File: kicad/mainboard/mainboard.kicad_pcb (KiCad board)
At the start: 2 copper layers, 40 x 58 mm, 32 parts, among them J1 USB_C_Receptacle_USB2.0_16P, J2 Conn_01x07_Socket, J3 Conn_01x06_Socket, J4 Conn_01x03_Socket, J5 Conn_01x07_Socket, SW1 FSM2JSMAATR, SW2 FSM2JSMAATR, U1 TPD1E05U06DYA, U2 TPD1E05U06DYA, U3 ESP32-S3-WROOM-1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

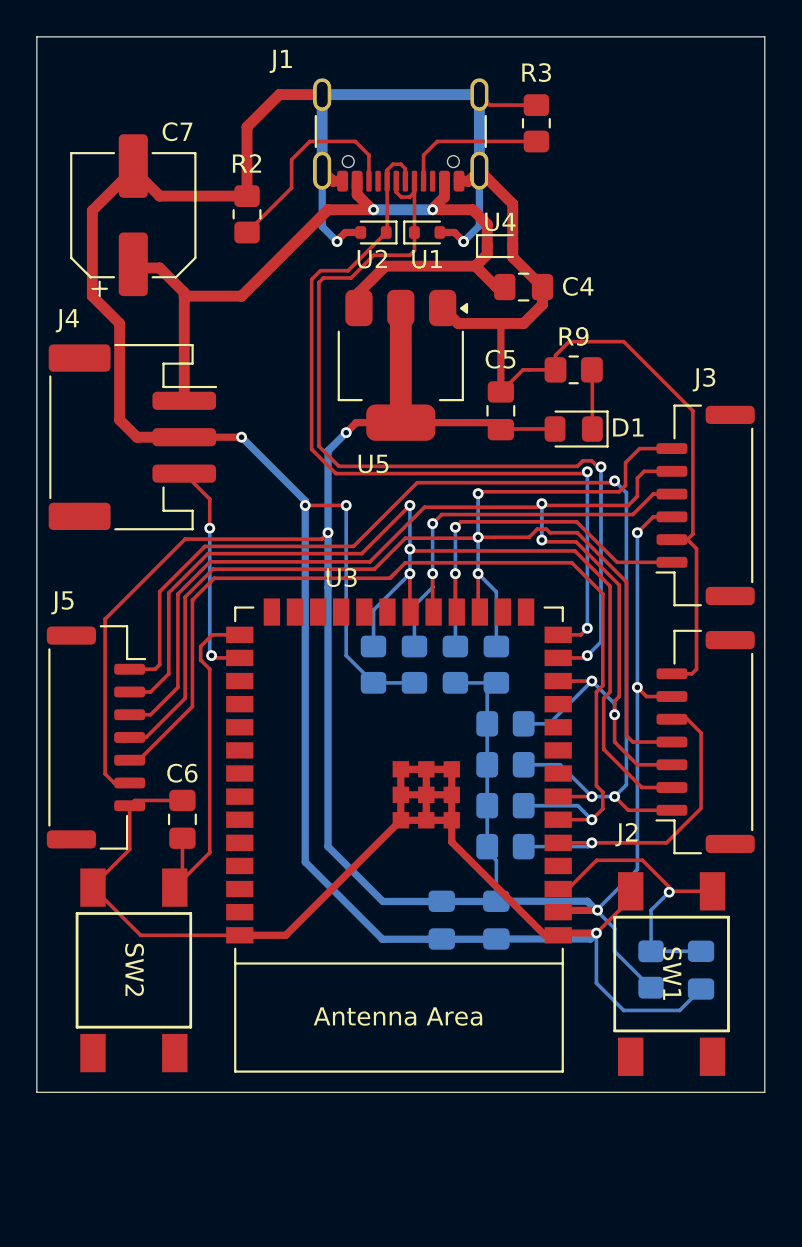
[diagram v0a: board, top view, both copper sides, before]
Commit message: via/trace cleanup, larger via for 5v2a
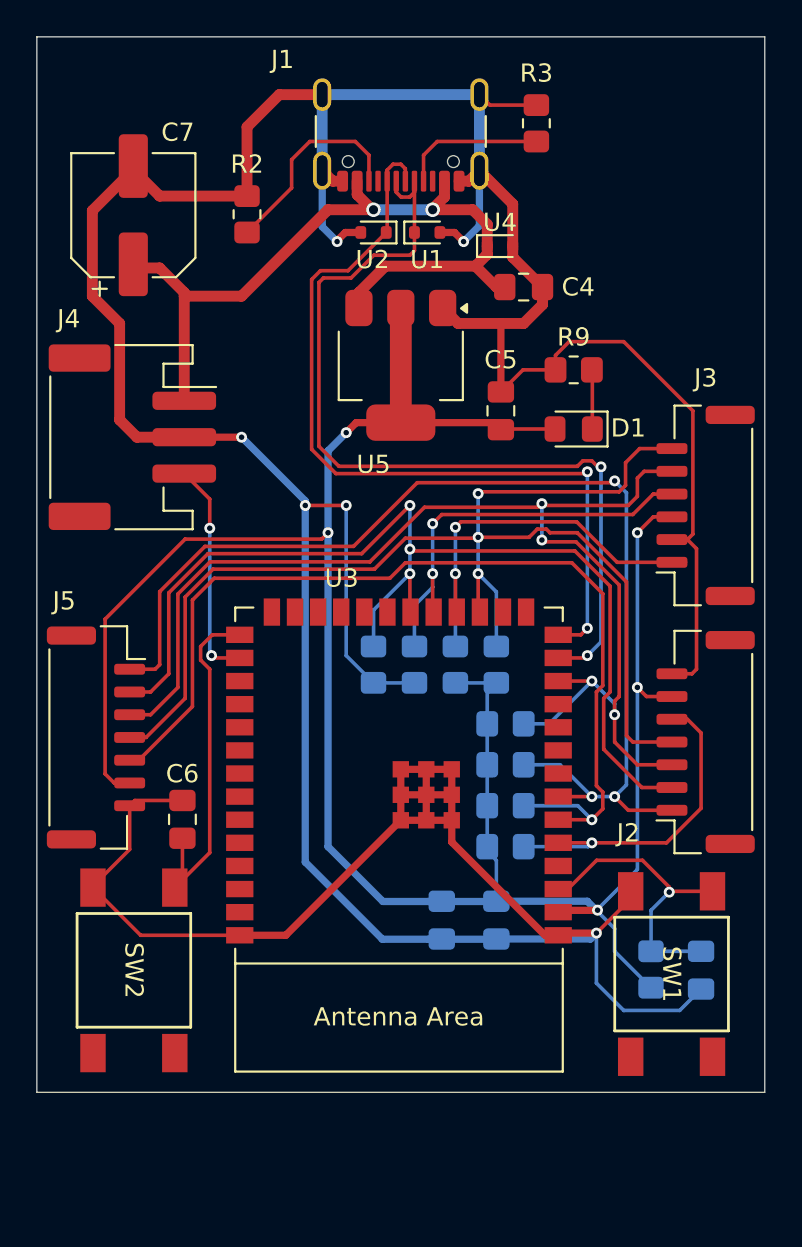
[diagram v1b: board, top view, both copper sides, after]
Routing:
- net +3.3V: track 131.0 -> 130.2 mm
- net GND: track 249.9 -> 249.3 mm
- net SMCLK: track 71.5 -> 71.0 mm
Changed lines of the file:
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@@
-	)
-	(segment
-		(start 136.88215 110.7034)
-		(end 136.88215 110.574088)
-		(width 0.2)
-		(layer "F.Cu")
-		(net 1)
 	)
 	(segment
@@
 	)
 	(segment
-		(start 109.35 106)
-		(end 109.75 106)
-		(width 0.2)
-		(layer "F.Cu")
-		(net 1)
-	)
-	(segment
 		(start 124.25 106.8)
 		(end 124.25 104)
@@
 	)
 	(segment
-		(start 132.75 82.05)
-		(end 131.3 82.05)
+		(start 130.9625 82.05)
+		(end 132.75 82.05)
 		(width 0.2)
 		(layer "F.Cu")
@@
 	)
 	(segment
-		(start 131.3 82.05)
-		(end 130.9625 82.05)
-		(width 0.2)
-		(layer "F.Cu")
-		(net 1)
-	)
-	(segment
 		(start 115.8 72.5)
 		(end 111 72.5)
@@
 		(end 128.57 71.105)
 		(width 0.6)
-		(layer "B.Cu")
-		(net 1)
-	)
-	(segment
-		(start 120.7 75)
-		(end 120.75 75)
-		(width 0.4)
 		(layer "B.Cu")
 		(net 1)
@@
 	)
 	(segment
-		(start 123.7 85.5)
-		(end 124.25 84.95)
-		(width 0.4)
-		(layer "F.Cu")
-		(net 3)
-	)
-	(segment
 		(start 129.7875 85.3)
 		(end 129.75 85.3375)
@@
 	(segment
 		(start 120.25 108.25)
-		(end 120.25 94)
+		(end 120.25 86.5)
 		(width 0.4)
 		(layer "B.Cu")
@@
 	)
 	(segment
-		(start 120.25 94)
-		(end 120.25 86.5)
-		(width 0.4)
-		(layer "B.Cu")
-		(net 3)
-	)
-	(segment
 		(start 127.25 99.25)
 		(end 129.5 99.25)
@@
 	)
 	(segment
-		(start 128.6 76.1)
-		(end 128.35 76.35)
+		(start 128.35 76.35)
+		(end 129 75.7)
 		(width 0.6)
 		(layer "F.Cu")
@@
 	)
 	(segment
-		(start 129 75.7)
-		(end 128.6 76.1)
-		(width 0.6)
-		(layer "F.Cu")
-		(net 4)
-	)
-	(segment
 		(start 129.5 77.5)
 		(end 129.9625 77.5)
@@
 	(via
 		(at 126 73.25)
-		(size 0.6)
-		(drill 0.3)
+		(size 0.8)
+		(drill 0.5)
 		(layers "F.Cu" "B.Cu")
 		(net 4)
@@
 	(via
 		(at 122.75 73.25)
-		(size 0.6)
-		(drill 0.3)
+		(size 0.8)
+		(drill 0.5)
 		(layers "F.Cu" "B.Cu")
 		(net 4)
@@
 	)
 	(segment
-		(start 111.75 110.419375)
-		(end 111.830625 110.5)
-		(width 0.2)
-		(layer "F.Cu")
-		(net 5)
-	)
-	(segment
 		(start 113.75 98.498529)
 		(end 113.75 108.580625)
@@
 	)
 	(segment
-		(start 128.595 94.83)
-		(end 128.595 95.36)
-		(width 0.2)
-		(layer "F.Cu")
-		(net 15)
-	)
-	(segment
 		(start 131.301471 91.25)
 		(end 131.751471 90.8)
@@
 	)
 	(segment
-		(start 123.950735 93.200735)
+		(start 123.65147 93.5)
 		(end 124.501471 92.65)
 		(width 0.2)
@@
 	)
 	(segment
-		(start 123.651471 93.5)
-		(end 123.950735 93.200735)
-		(width 0.2)
-		(layer "F.Cu")
-		(net 18)
-	)
-	(segment
 		(start 133.65 92.65)
 		(end 135.35 94.35)
@@
 		(width 0.2)
 		(layer "F.Cu")
-		(net 18)
-	)
-	(segment
-		(start 123.65147 93.5)
-		(end 123.950735 93.200735)
-		(width 0.2)
-		(layer "F.Cu")

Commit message: adjust edge cut
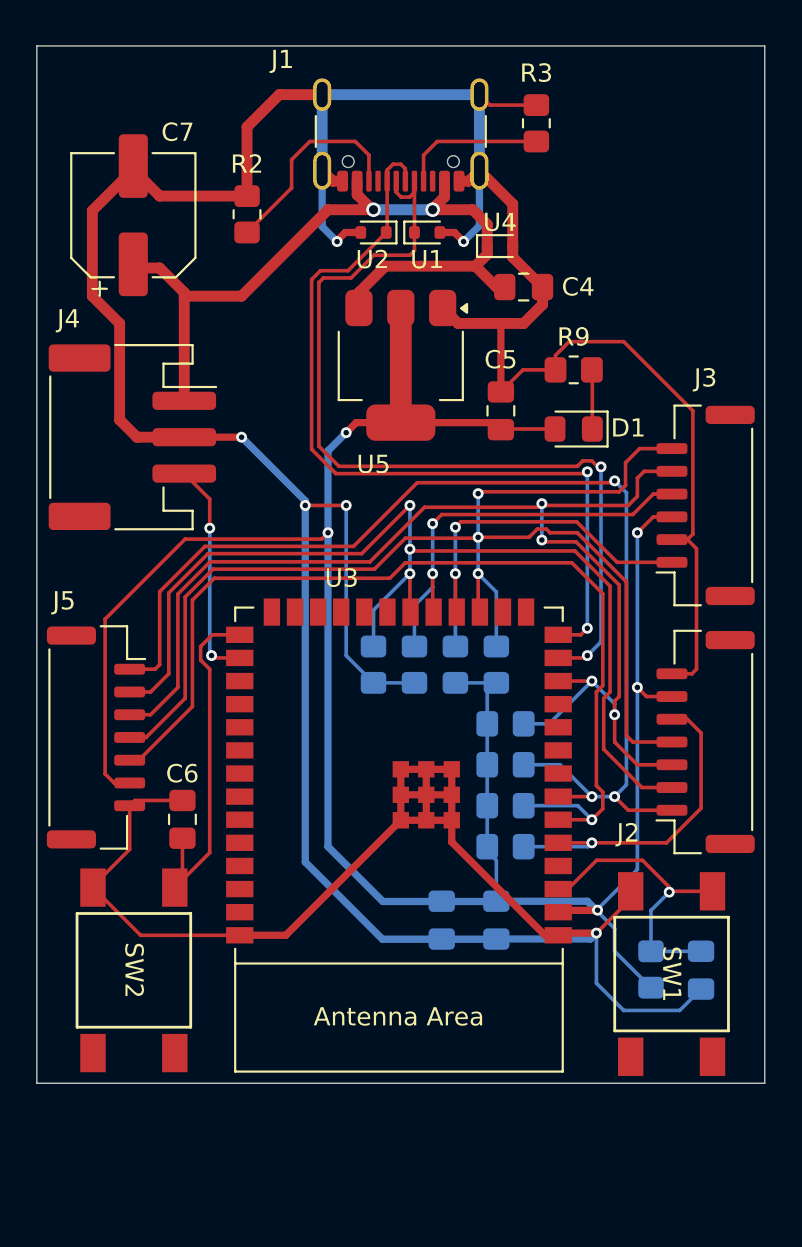
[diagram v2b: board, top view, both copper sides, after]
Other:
- board size 40 x 58 mm -> 40 x 57 mm
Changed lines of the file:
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@@
 	)
 	(gr_line
-		(start 144.25 60.25)
-		(end 124.25 60.25)
+		(start 144.25 65.25)
+		(end 124.25 65.25)
 		(stroke
 			(width 0.1)
@@
 	)
 	(gr_line
-		(start 124.25 60.25)
-		(end 124.25 57.75)
+		(start 124.25 65.25)
+		(end 124.25 62.75)
 		(stroke
 			(width 0.1)
@@
 	)
 	(gr_rect
-		(start 104.25 63.75)
-		(end 144.25 121.75)
+		(start 104.25 64.25)
+		(end 144.25 121.25)
 		(stroke
 			(width 0.05)

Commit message: Add logo
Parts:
- added G***: LOGO, Logo:Snep, F.Cu at (139.0, 69.0)

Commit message: fix erc
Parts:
- moved SW1 0.20 mm to (141.4, 110.5)
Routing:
- net EN: track 16.5 -> 17.2 mm
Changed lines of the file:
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@@
 		(tags "USB C Type-C Receptacle SMD USB 2.0 16P 16C USB4105-15-A USB4105-15-A-060 USB4105-15-A-120 USB4105-GF-A USB4105-GF-A-060 USB4105-GF-A-120")
 		(property "Reference" "J1"
-			(at 6.5 3 0)
+			(at 6.5 2.5 0)
 			(unlocked yes)
 			(layer "F.SilkS")
@@
 		(tags "capacitor handsolder")
 		(property "Reference" "C6"
-			(at -2.5 0 180)
+			(at -2.75 0 180)
 			(layer "F.SilkS")
 			(effects
@@
 		(tags "connector JST GH horizontal")
 		(property "Reference" "J2"
-			(at -5 -4.25 180)
+			(at 6 -4.25 180)
 			(layer "F.SilkS")
 			(effects
@@
 	(footprint "FSM2JSMAATR:SWITCH_FSM2JSMAA_TYC"
 		(layer "F.Cu")
-		(at 141.37795 110.7034 -90)
+		(at 141.37795 110.5 -90)
 		(tags "FSM2JSMAATR ")
 		(property "Reference" "SW1"
@@
 		(tags "resistor handsolder")
 		(property "Reference" "R11"
-			(at -2.75 -0.5 0)
+			(at -0.25 -2.5 0)
 			(layer "B.SilkS")
 			(effects
@@
 		(tags "resistor handsolder")
 		(property "Reference" "R12"
-			(at -2.75 0.25 0)
+			(at -2.75 0 0)
 			(layer "B.SilkS")
 			(effects
@@
 	)
 	(segment
+		(start 136.88215 111.11785)
+		(end 136.88215 110.5)
+		(width 0.2)
+		(layer "F.Cu")
+		(net 1)
+	)
+	(segment
 		(start 125.65 104)
 		(end 125.65 106.8)
@@
 	)
 	(segment
+		(start 135 113)
+		(end 136.88215 111.11785)
+		(width 0.2)
+		(layer "F.Cu")
+		(net 1)
+	)
+	(segment
 		(start 131.7 67.5)
 		(end 129.145 67.5)
@@
 	)
 	(segment
-		(start 136.88215 110.7034)
-		(end 136.88215 111.11785)
-		(width 0.2)
-		(layer "F.Cu")
-		(net 1)
-	)
-	(segment
 		(start 130.4 75.8625)
 		(end 132.0375 77.5)
@@
 	)
 	(segment
-		(start 136.88215 111.11785)
-		(end 135 113)
-		(width 0.2)
-		(layer "F.Cu")
-		(net 1)
-	)
-	(segment
 		(start 107.3 73.3)
 		(end 107.3 78)
@@
 	)
 	(segment
-		(start 137.53135 109)
-		(end 135.01 109)
+		(start 139.25 110.5)
+		(end 141.37795 110.5)
 		(width 0.2)
 		(layer "F.Cu")
@@
 	(segment
 		(start 139 110.75)
-		(end 139 110.46865)
+		(end 139 109.75)
 		(width 0.2)
 		(layer "F.Cu")
@@
 	)
 	(segment
-		(start 139.0466 110.7034)
-		(end 141.37795 110.7034)
+		(start 139 110.75)
+		(end 139.25 110.5)
 		(width 0.2)
 		(layer "F.Cu")
@@
 	)
 	(segment
-		(start 139 110.75)
-		(end 139.0466 110.7034)
+		(start 138 108.75)
+		(end 135.26 108.75)
 		(width 0.2)
 		(layer "F.Cu")
@@
 	)
 	(segment
-		(start 139 110.46865)
-		(end 137.53135 109)
+		(start 139 109.75)
+		(end 138 108.75)
 		(width 0.2)
 		(layer "F.Cu")
@@
 	)
 	(segment
-		(start 135.01 109)
-		(end 133.43 110.58)
+		(start 133.43 110.58)
+		(end 132.9 110.58)
 		(width 0.2)
 		(layer "F.Cu")
@@
 	)
 	(segment
-		(start 133.43 110.58)
-		(end 132.9 110.58)
+		(start 135.26 108.75)
+		(end 133.43 110.58)
 		(width 0.2)
 		(layer "F.Cu")

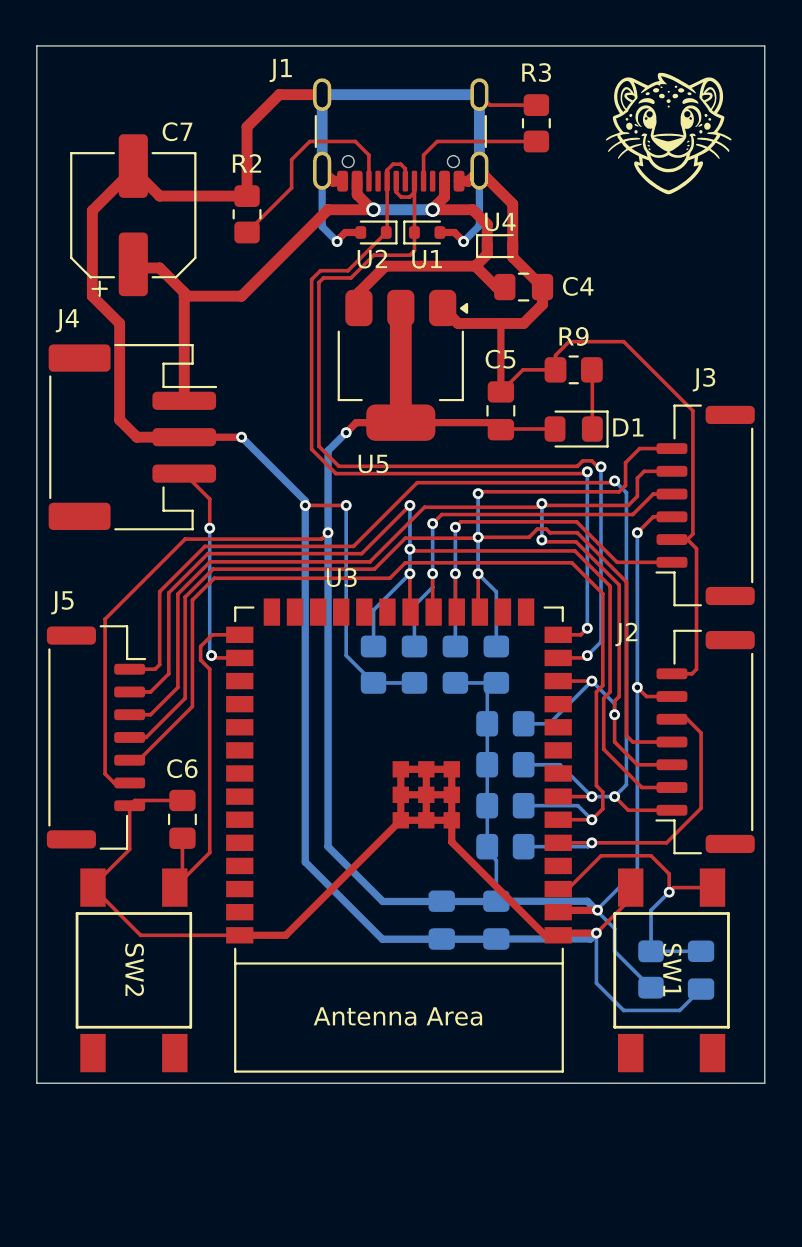
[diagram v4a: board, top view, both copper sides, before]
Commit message: add mountholes
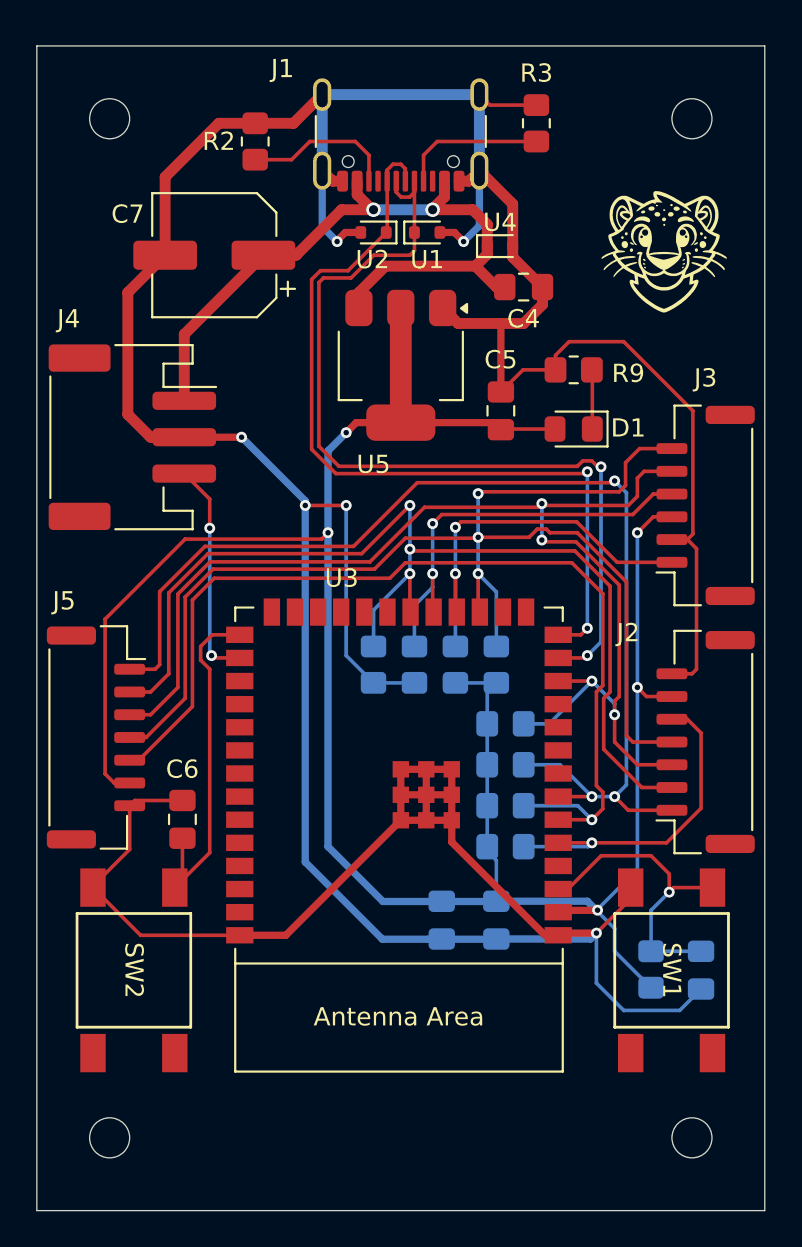
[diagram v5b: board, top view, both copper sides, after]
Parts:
- added H1: MountingHole, MountingHole:MountingHole_2.2mm_M2, F.Cu at (140.2, 68.2)
- added H2: MountingHole, MountingHole:MountingHole_2.2mm_M2, F.Cu at (108.2, 68.2)
- added H3: MountingHole, MountingHole:MountingHole_2.2mm_M2, F.Cu at (108.2, 124.2)
- added H4: MountingHole, MountingHole:MountingHole_2.2mm_M2, F.Cu at (140.2, 124.2)
- moved G*** 6.50 mm to (138.8, 75.5)
- moved C7 4.96 mm to (114.0, 75.8), turned to 180 degrees
- moved R2 4.03 mm to (116.2, 69.5)
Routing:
- net GND: track 249.5 -> 242.8 mm
- net +5V: track 44.6 -> 39.8 mm
- net Net-(J1-CC2): track 11.4 -> 8.40 mm
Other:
- board size 40 x 57 mm -> 40 x 64 mm

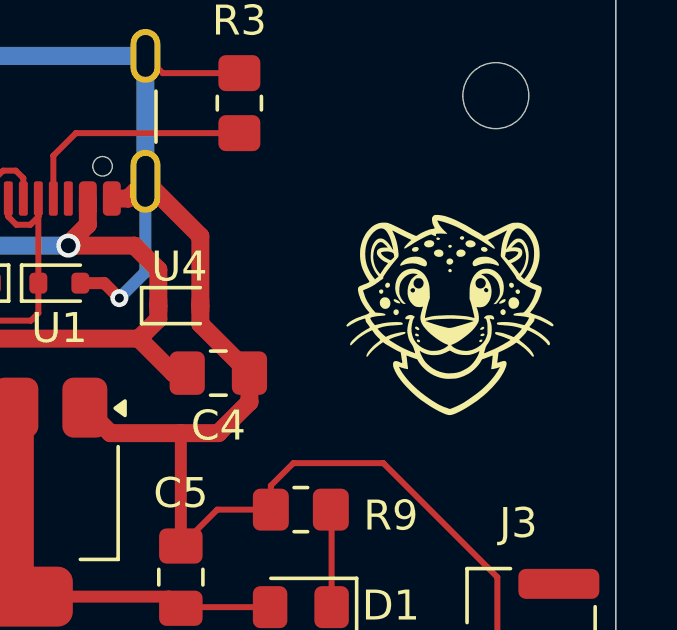
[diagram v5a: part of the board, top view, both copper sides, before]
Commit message: solder mask logo
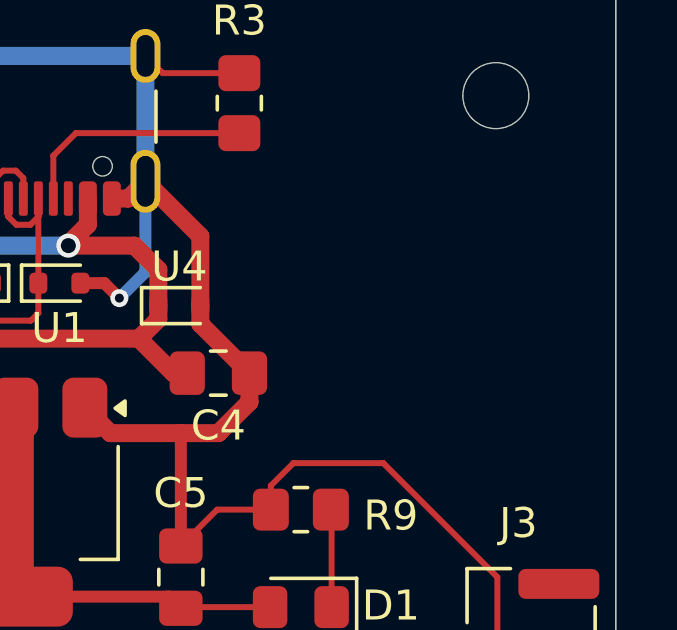
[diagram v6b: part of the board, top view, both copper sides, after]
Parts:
- removed the G*** at (138.8, 75.5)
- added G***: LOGO, Logo:Snep_Copper, F.Cu at (138.8, 75.5)
